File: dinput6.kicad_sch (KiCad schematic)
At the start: 34 parts, among them U4 74HC14PW,118

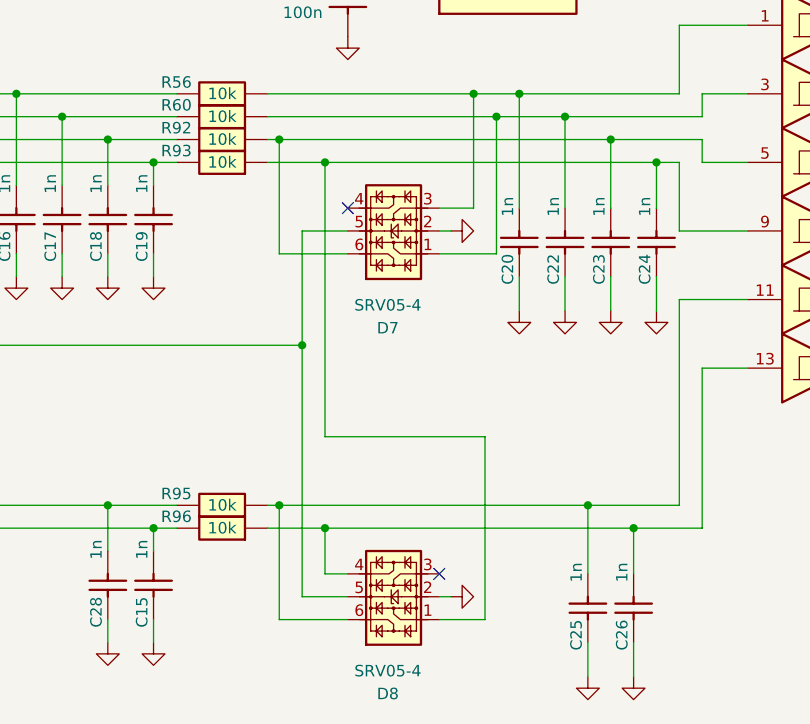
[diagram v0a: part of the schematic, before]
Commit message: srv05 value fix
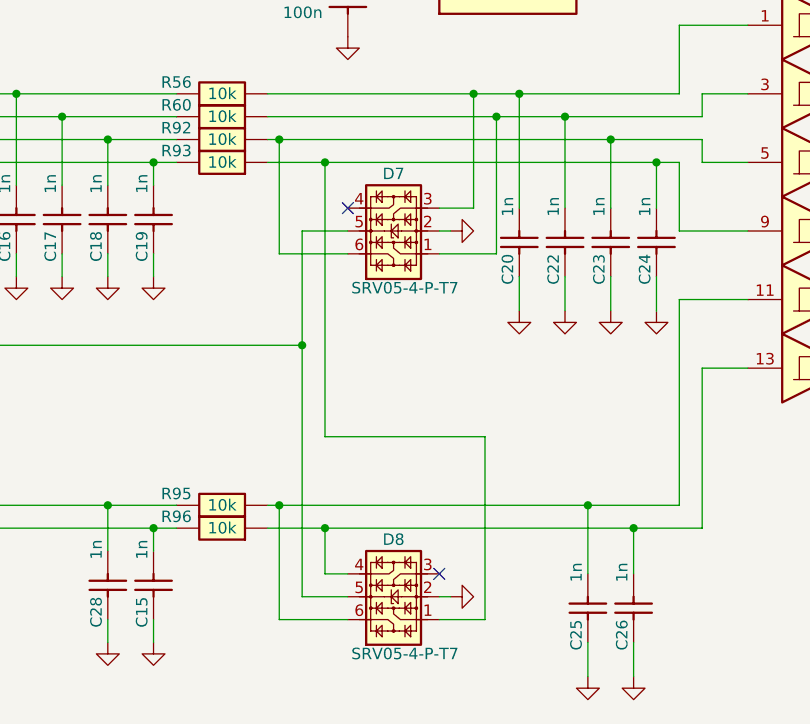
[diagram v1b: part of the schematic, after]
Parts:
- D7, D8: value SRV05-4 -> SRV05-4-P-T7
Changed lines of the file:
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@@
   (symbol (lib_id "Power_Protection:NUP4202") (at 146.05 92.71 90) (unit 1)
     (in_bom yes) (on_board yes) (dnp no)
-    (property "Reference" "D7" (at 145.415 103.505 90)
-      (effects (font (size 1.27 1.27)))
-    )
-    (property "Value" "SRV05-4" (at 145.415 100.965 90)
+    (property "Reference" "D7" (at 146.05 86.36 90)
+      (effects (font (size 1.27 1.27)))
+    )
+    (property "Value" "SRV05-4-P-T7" (at 147.32 99.06 90)
       (effects (font (size 1.27 1.27)))
     )
@@
   (symbol (lib_id "Power_Protection:NUP4202") (at 146.05 133.35 90) (unit 1)
     (in_bom yes) (on_board yes) (dnp no)
-    (property "Reference" "D8" (at 145.415 144.145 90)
-      (effects (font (size 1.27 1.27)))
-    )
-    (property "Value" "SRV05-4" (at 145.415 141.605 90)
-      (effects (font (size 1.27 1.27)))
-    )
+    (property "Reference" "D8" (at 146.05 127 90)
+      (effects (font (size 1.27 1.27)))
+    )
+    (property "Value" "SRV05-4-P-T7" (at 147.32 139.7 90)
+      (effects (font (size 1.27 1.27)))
+    )

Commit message: Warnings fix
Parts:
- C15, C16, C17, C18, C19, C20, C22, C23, C24, C25, C26, C28: LCSC C106247 -> C1588
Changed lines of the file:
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@@
       (effects (font (size 1.27 1.27)) hide)
     )
-    (property "LCSC" "C106247" (at 114.3 132.08 0)
+    (property "LCSC" "C1588" (at 114.3 132.08 0)
       (effects (font (size 1.27 1.27)) hide)
     )
@@
       (effects (font (size 1.27 1.27)) hide)
     )
-    (property "LCSC" "C106247" (at 119.38 91.44 0)
+    (property "LCSC" "C1588" (at 119.38 91.44 0)
       (effects (font (size 1.27 1.27)) hide)
     )
@@
       (effects (font (size 1.27 1.27)) hide)
     )
-    (property "LCSC" "C106247" (at 160.02 93.98 0)
+    (property "LCSC" "C1588" (at 160.02 93.98 0)
       (effects (font (size 1.27 1.27)) hide)
     )
@@
       (effects (font (size 1.27 1.27)) hide)
     )
-    (property "LCSC" "C106247" (at 104.14 91.44 0)
+    (property "LCSC" "C1588" (at 104.14 91.44 0)
       (effects (font (size 1.27 1.27)) hide)
     )
@@
       (effects (font (size 1.27 1.27)) hide)
     )
-    (property "LCSC" "C106247" (at 165.1 93.98 0)
+    (property "LCSC" "C1588" (at 165.1 93.98 0)
       (effects (font (size 1.27 1.27)) hide)
     )
@@
       (effects (font (size 1.27 1.27)) hide)
     )
-    (property "LCSC" "C106247" (at 119.38 132.08 0)
+    (property "LCSC" "C1588" (at 119.38 132.08 0)
       (effects (font (size 1.27 1.27)) hide)
     )
@@
       (effects (font (size 1.27 1.27)) hide)
     )
-    (property "LCSC" "C106247" (at 170.18 93.98 0)
+    (property "LCSC" "C1588" (at 170.18 93.98 0)
       (effects (font (size 1.27 1.27)) hide)
     )
@@
       (effects (font (size 1.27 1.27)) hide)
     )
-    (property "LCSC" "C106247" (at 109.22 91.44 0)
+    (property "LCSC" "C1588" (at 109.22 91.44 0)
       (effects (font (size 1.27 1.27)) hide)
     )
@@
       (effects (font (size 1.27 1.27)) hide)
     )
-    (property "LCSC" "C106247" (at 172.72 134.62 0)
+    (property "LCSC" "C1588" (at 172.72 134.62 0)
       (effects (font (size 1.27 1.27)) hide)
     )
@@
       (effects (font (size 1.27 1.27)) hide)
     )
-    (property "LCSC" "C106247" (at 167.64 134.62 0)
+    (property "LCSC" "C1588" (at 167.64 134.62 0)
       (effects (font (size 1.27 1.27)) hide)
     )
@@
       (effects (font (size 1.27 1.27)) hide)
     )
-    (property "LCSC" "C106247" (at 175.26 93.98 0)
+    (property "LCSC" "C1588" (at 175.26 93.98 0)
       (effects (font (size 1.27 1.27)) hide)
     )
@@
       (effects (font (size 1.27 1.27)) hide)
     )
-    (property "LCSC" "C106247" (at 114.3 91.44 0)
-      (effects (font (size 1.27 1.27)) hide)
-    )
+    (property "LCSC" "C1588" (at 114.3 91.44 0)
+      (effects (font (size 1.27 1.27)) hide)
+    )
